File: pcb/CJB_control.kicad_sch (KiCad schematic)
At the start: 23 parts, among them J2 Micro_SD_Card, J3 Conn_01x06_Socket, J4 Conn_01x06_Socket, Q2 AO3400A, SW2 SW_MEC_5E, SW3 SW_MEC_5E, U4 ESP32-WROOM-32UE-R2

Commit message: Add BOOT and RESET jumper
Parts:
- added J5, J6: Conn_01x02_Pin, Connector_PinHeader_2.54mm:PinHeader_1x02_P2.54mm_Vertical, symbol Connector:Conn_01x02_Pin
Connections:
- net GND: now also J5.1 (Pin_1), J6.1 (Pin_1)
- net at C9.2, R13.2, SW3.1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: now also J5.2 (Pin_2)
- net at R12.1, SW2.1, SW2.2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: now also J6.2 (Pin_2)
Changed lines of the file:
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@@
   (junction (at 111.76 57.15) (diameter 0) (color 0 0 0 0)
+  )
+  (junction (at 49.53 59.69) (diameter 0) (color 0 0 0 0)
   )
   (junction (at 168.91 80.01) (diameter 0) (color 0 0 0 0)
@@
     (stroke (width 0) (type default))
   )
+  (wire (pts (xy 109.22 57.15) (xy 111.76 57.15))
+    (stroke (width 0) (type default))
+  )
   (wire (pts (xy 92.71 138.43) (xy 96.52 138.43))
     (stroke (width 0) (type default))
@@
     (stroke (width 0) (type default))
   )
+  (wire (pts (xy 109.22 46.99) (xy 109.22 57.15))
+    (stroke (width 0) (type default))
+  )
   (wire (pts (xy 93.98 52.07) (xy 93.98 54.61))
     (stroke (width 0) (type default))
@@
     (stroke (width 0) (type default))
   )
+  (wire (pts (xy 52.07 50.8) (xy 52.07 49.53))
+    (stroke (width 0) (type default))
+  )
   (wire (pts (xy 55.88 59.69) (xy 55.88 62.23))
     (stroke (width 0) (type default))
@@
     (stroke (width 0) (type default))
   )
+  (wire (pts (xy 49.53 49.53) (xy 49.53 59.69))
+    (stroke (width 0) (type default))
+  )
   (wire (pts (xy 163.83 74.93) (xy 186.69 74.93))
     (stroke (width 0) (type default))
@@
   )
   (wire (pts (xy 130.81 115.57) (xy 133.35 118.11))
+    (stroke (width 0) (type default))
+  )
+  (wire (pts (xy 106.68 48.26) (xy 106.68 46.99))
     (stroke (width 0) (type default))
   )
@@
     )
   )
+  (symbol (lib_id "Connector:Conn_01x02_Pin") (at 52.07 44.45 270) (unit 1)
+    (in_bom yes) (on_board yes) (dnp no)
+    (property "Reference" "J5" (at 50.8 43.18 90)
+      (effects (font (size 1.27 1.27)))
+    )
+    (property "Value" "Conn_01x02_Pin" (at 54.61 45.085 0)
+      (effects (font (size 1.27 1.27)) hide)
+    )
+    (property "Footprint" "Connector_PinHeader_2.54mm:PinHeader_1x02_P2.54mm_Vertical" (at 52.07 44.45 0)
+      (effects (font (size 1.27 1.27)) hide)
+    )
+    (property "Datasheet" "~" (at 52.07 44.45 0)
+      (effects (font (size 1.27 1.27)) hide)
+    )
+    (pin "1")
+    (pin "2")
+    (instances
+      (project "CJB"
+        (path "/9334361a-f7a5-4302-90e9-4b89798c8fc6/f854ee70-c58b-43a6-b79d-436304fbc428"
+          (reference "J5") (unit 1)
+        )
+      )
+    )
+  )
   (symbol (lib_id "Device:R") (at 161.29 66.04 180) (unit 1)
     (in_bom yes) (on_board yes) (dnp no)
@@
         (path "/9334361a-f7a5-4302-90e9-4b89798c8fc6/f854ee70-c58b-43a6-b79d-436304fbc428"
           (reference "#PWR036") (unit 1)
+        )
+      )
+    )
+  )
+  (symbol (lib_id "power:GND") (at 52.07 50.8 0) (unit 1)
+    (in_bom yes) (on_board yes) (dnp no)
+    (property "Reference" "#PWR0124" (at 52.07 57.15 0)
+      (effects (font (size 1.27 1.27)) hide)
+    )
+    (property "Value" "GND" (at 52.07 55.88 90)
+      (effects (font (size 1.27 1.27)))
+    )
+    (property "Footprint" "" (at 52.07 50.8 0)
+      (effects (font (size 1.27 1.27)) hide)
+    )
+    (property "Datasheet" "" (at 52.07 50.8 0)
+      (effects (font (size 1.27 1.27)) hide)
+    )
+    (pin "1")
+    (instances
+      (project "CJB"
+        (path "/9334361a-f7a5-4302-90e9-4b89798c8fc6/f854ee70-c58b-43a6-b79d-436304fbc428"
+          (reference "#PWR0124") (unit 1)
         )
       )
@@
   (symbol (lib_id "Device:R") (at 111.76 50.8 180) (unit 1)
     (in_bom yes) (on_board yes) (dnp no)
-    (property "Reference" "R12" (at 109.22 50.8 90)
+    (property "Reference" "R12" (at 114.3 49.53 90)
       (effects (font (size 1.27 1.27)))
     )
@@
   )
   (symbol (lib_id "power:+3V3") (at 55.88 46.99 0) (unit 1)
-    (in_bom yes) (on_board yes) (dnp no) (fields_autoplaced)
+    (in_bom yes) (on_board yes) (dnp no)
     (property "Reference" "#PWR026" (at 55.88 50.8 0)
       (effects (font (size 1.27 1.27)) hide)
     )
-    (property "Value" "+3V3" (at 55.88 41.91 0)
+    (property "Value" "+3V3" (at 55.88 40.64 90)
       (effects (font (size 1.27 1.27)))
     )
@@
         (path "/9334361a-f7a5-4302-90e9-4b89798c8fc6/f854ee70-c58b-43a6-b79d-436304fbc428"
           (reference "#PWR026") (unit 1)
+        )
+      )
+    )
+  )
+  (symbol (lib_id "power:GND") (at 106.68 48.26 0) (mirror y) (unit 1)
+    (in_bom yes) (on_board yes) (dnp no)
+    (property "Reference" "#PWR0125" (at 106.68 54.61 0)
+      (effects (font (size 1.27 1.27)) hide)
+    )
+    (property "Value" "GND" (at 106.68 53.34 90)
+      (effects (font (size 1.27 1.27)))
+    )
+    (property "Footprint" "" (at 106.68 48.26 0)
+      (effects (font (size 1.27 1.27)) hide)
+    )
+    (property "Datasheet" "" (at 106.68 48.26 0)
+      (effects (font (size 1.27 1.27)) hide)
+    )
+    (pin "1")
+    (instances
+      (project "CJB"
+        (path "/9334361a-f7a5-4302-90e9-4b89798c8fc6/f854ee70-c58b-43a6-b79d-436304fbc428"
+          (reference "#PWR0125") (unit 1)
         )
       )
@@
   )
   (symbol (lib_id "power:+3V3") (at 111.76 44.45 0) (unit 1)
-    (in_bom yes) (on_board yes) (dnp no) (fields_autoplaced)
+    (in_bom yes) (on_board yes) (dnp no)
     (property "Reference" "#PWR025" (at 111.76 48.26 0)
       (effects (font (size 1.27 1.27)) hide)
     )
-    (property "Value" "+3V3" (at 111.76 39.37 0)
+    (property "Value" "+3V3" (at 111.76 38.1 90)
       (effects (font (size 1.27 1.27)))
     )
@@
         )
       )
+    )
+  )
+  (symbol (lib_id "Connector:Conn_01x02_Pin") (at 106.68 41.91 90) (mirror x) (unit 1)
+    (in_bom yes) (on_board yes) (dnp no)
+    (property "Reference" "J6" (at 107.95 40.64 90)
+      (effects (font (size 1.27 1.27)))
+    )
+    (property "Value" "Conn_01x02_Pin" (at 104.14 42.545 0)
+      (effects (font (size 1.27 1.27)) hide)
+    )
+    (property "Footprint" "Connector_PinHeader_2.54mm:PinHeader_1x02_P2.54mm_Vertical" (at 106.68 41.91 0)
+      (effects (font (size 1.27 1.27)) hide)
+    )
+    (property "Datasheet" "~" (at 106.68 41.91 0)
+      (effects (font (size 1.27 1.27)) hide)
+    )
+    (pin "1")
+    (pin "2")
+    (instances
+      (project "CJB"
+        (path "/9334361a-f7a5-4302-90e9-4b89798c8fc6/f854ee70-c58b-43a6-b79d-436304fbc428"
+          (reference "J6") (unit 1)
+        )
+      )

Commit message: Fix boot and power issue
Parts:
- added J7: Conn_01x02_Pin, Connector_PinHeader_2.54mm:PinHeader_1x02_P2.54mm_Vertical, symbol Connector:Conn_01x02_Pin
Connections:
- net +3V3: now also J7.2 (Pin_2); no longer R16.2
- new net: J7.1 (Pin_1), R16.2
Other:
- moved on the sheet: R15, R16

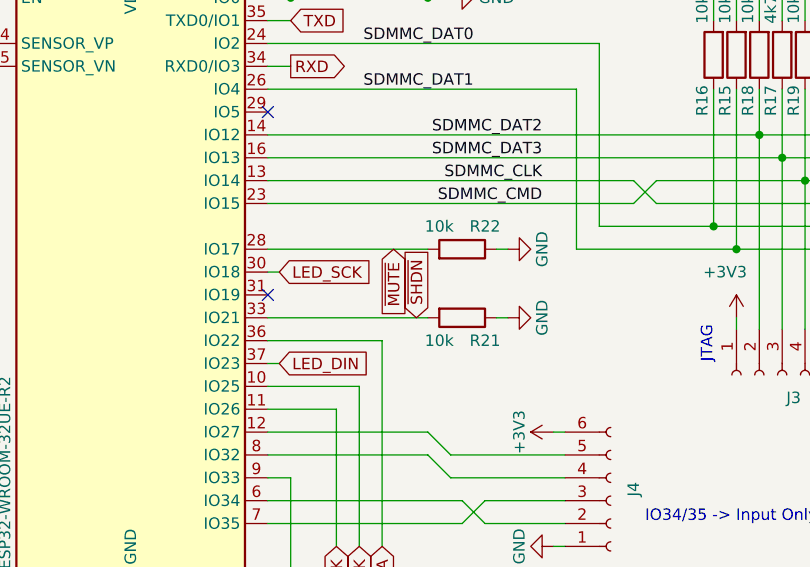
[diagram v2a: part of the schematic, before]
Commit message: Change SHDN and MUTE pins
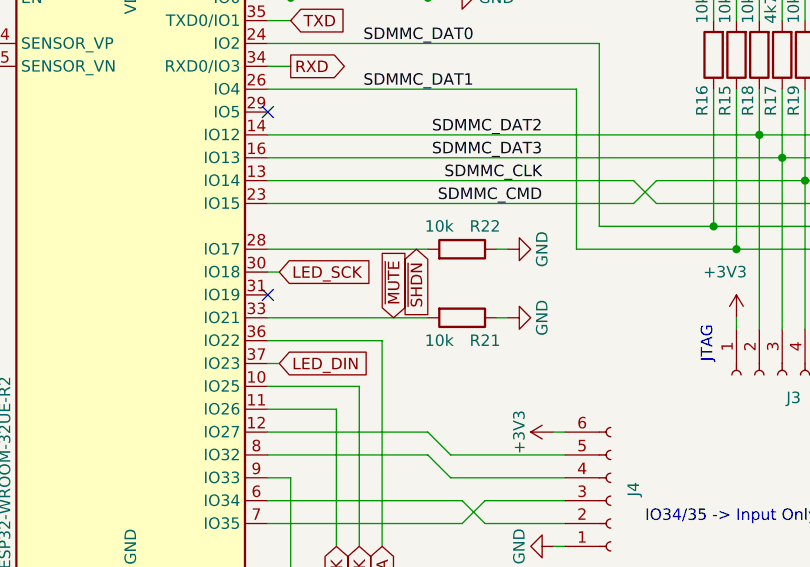
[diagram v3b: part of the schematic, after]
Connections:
- net ~{MUTE}: now also R21.2, U4.33 (IO21); no longer R22.2, U4.28 (IO17)
- net ~{SHDN}: now also R22.2, U4.28 (IO17); no longer R21.2, U4.33 (IO21)
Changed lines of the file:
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@@
     )
   )
-  (global_label "~{MUTE}" (shape input) (at 123.19 87.63 270) (fields_autoplaced)
-    (effects (font (size 1.27 1.27)) (justify right))
-    (property "Intersheetrefs" "${INTERSHEET_REFS}" (at 123.19 95.5137 90)
+  (global_label "~{MUTE}" (shape input) (at 123.19 95.25 90) (fields_autoplaced)
+    (effects (font (size 1.27 1.27)) (justify left))
+    (property "Intersheetrefs" "${INTERSHEET_REFS}" (at 123.19 87.3663 90)
       (effects (font (size 1.27 1.27)) (justify right) hide)
     )
@@
     )
   )
-  (global_label "~{SHDN}" (shape input) (at 125.73 95.25 90) (fields_autoplaced)
-    (effects (font (size 1.27 1.27)) (justify left))
-    (property "Intersheetrefs" "${INTERSHEET_REFS}" (at 125.73 87.1243 90)
+  (global_label "~{SHDN}" (shape input) (at 125.73 87.63 270) (fields_autoplaced)
+    (effects (font (size 1.27 1.27)) (justify right))
+    (property "Intersheetrefs" "${INTERSHEET_REFS}" (at 125.73 95.7557 90)
       (effects (font (size 1.27 1.27)) (justify left) hide)
     )

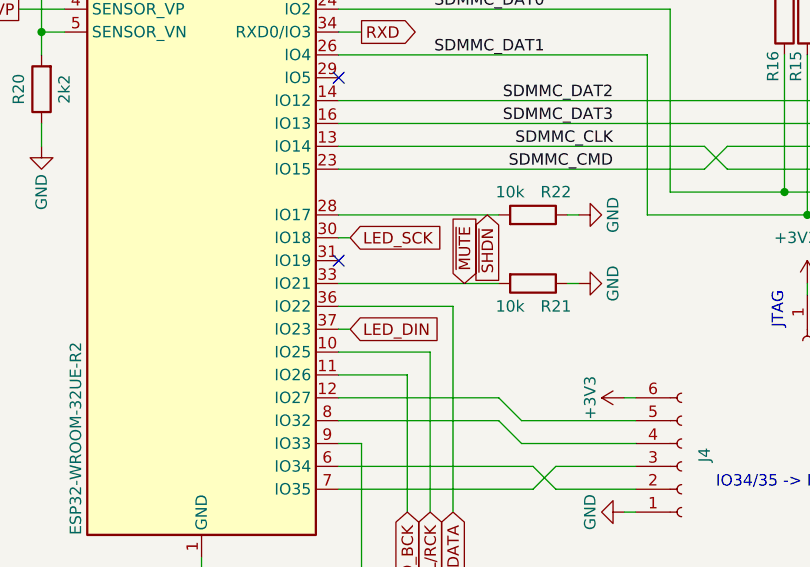
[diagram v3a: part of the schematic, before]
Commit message: Rename apa102 spi clk/data pins
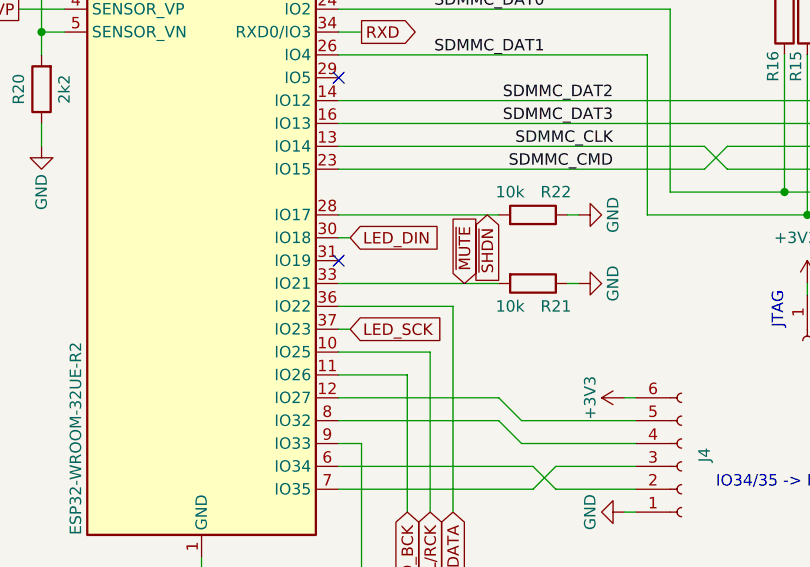
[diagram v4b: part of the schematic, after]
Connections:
- net LED_DIN: now also U4.30 (IO18); no longer U4.37 (IO23)
- net LED_SCK: now also U4.37 (IO23); no longer U4.30 (IO18)
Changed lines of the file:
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@@
     )
   )
-  (global_label "LED_DIN" (shape input) (at 110.49 100.33 0) (fields_autoplaced)
+  (global_label "LED_DIN" (shape input) (at 110.49 90.17 0) (fields_autoplaced)
     (effects (font (size 1.27 1.27)) (justify left))
-    (property "Intersheetrefs" "${INTERSHEET_REFS}" (at 121.0952 100.33 0)
+    (property "Intersheetrefs" "${INTERSHEET_REFS}" (at 121.0952 90.17 0)
       (effects (font (size 1.27 1.27)) (justify left) hide)
     )
@@
     )
   )
-  (global_label "LED_SCK" (shape input) (at 110.49 90.17 0) (fields_autoplaced)
+  (global_label "LED_SCK" (shape input) (at 110.49 100.33 0) (fields_autoplaced)
     (effects (font (size 1.27 1.27)) (justify left))
-    (property "Intersheetrefs" "${INTERSHEET_REFS}" (at 121.6394 90.17 0)
+    (property "Intersheetrefs" "${INTERSHEET_REFS}" (at 121.6394 100.33 0)
       (effects (font (size 1.27 1.27)) (justify left) hide)
     )
